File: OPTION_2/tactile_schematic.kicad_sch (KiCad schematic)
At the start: 58 parts, among them IC1 CY8C4145PVI-PS431, J1 Conn_01x02, J2 Conn_01x04, J3 Conn_01x04, J4 Conn_01x02, J5 Conn_ARM_SWD_TagConnect_TC203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

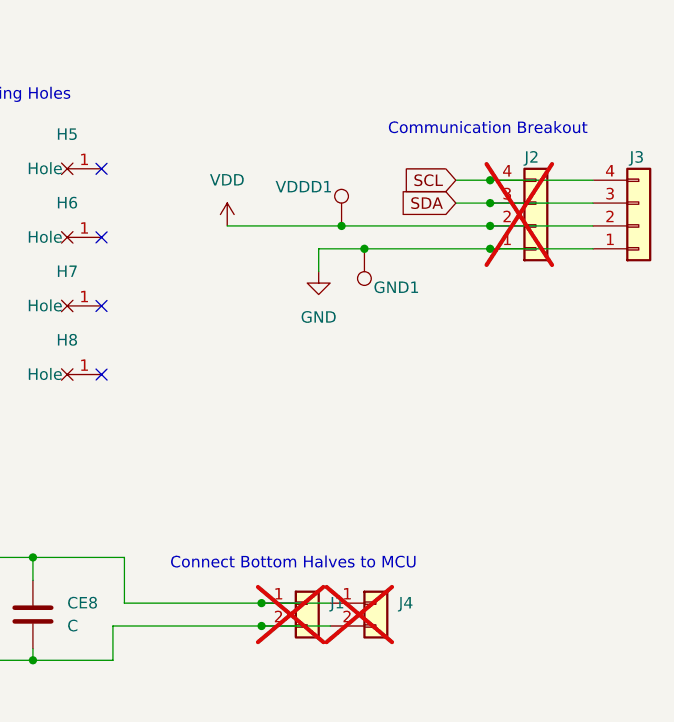
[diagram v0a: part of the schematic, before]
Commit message: three pcb trace configurations
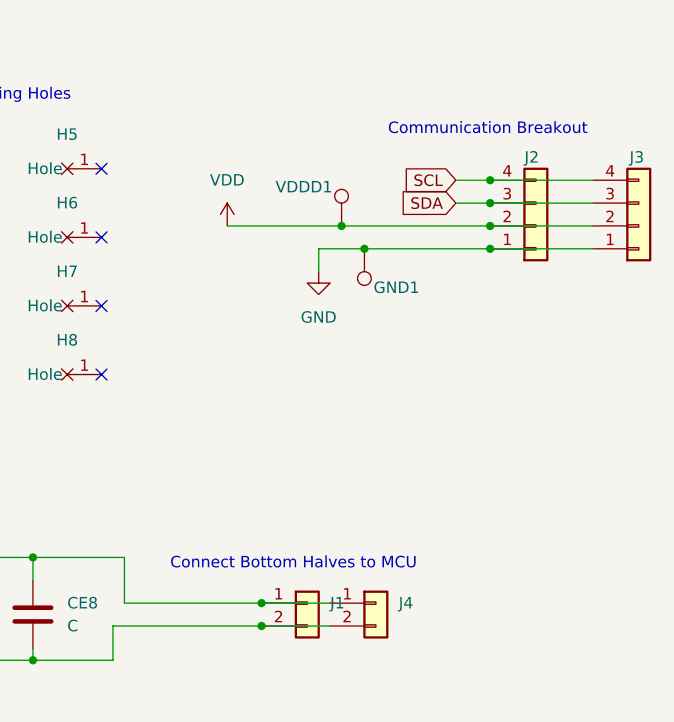
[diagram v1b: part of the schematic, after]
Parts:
- CE1, CE2, CE3, CE4: footprint ECE382N:COIL_GENERATOR -> ECE382N:04W_04S_COIL_BACK
- CE5, CE6, CE7, CE8: footprint ECE382N:COIL_GENERATOR -> ECE382N:04W_04S_COIL_FRONT
- J1, J2, J4: now fitted
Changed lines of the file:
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@@
 			)
 		)
-		(property "Footprint" "ECE382N:COIL_GENERATOR"
+		(property "Footprint" "ECE382N:04W_04S_COIL_BACK"
 			(at 39.0652 106.68 0)
 			(effects
@@
 			)
 		)
-		(property "Footprint" "ECE382N:COIL_GENERATOR"
+		(property "Footprint" "ECE382N:04W_04S_COIL_FRONT"
 			(at 192.7352 106.68 0)
 			(effects
@@
 		(in_bom yes)
 		(on_board yes)
-		(dnp yes)
+		(dnp no)
 		(fields_autoplaced yes)
 		(property "Reference" "J1"
@@
 			)
 		)
-		(property "Footprint" "ECE382N:COIL_GENERATOR"
+		(property "Footprint" "ECE382N:04W_04S_COIL_FRONT"
 			(at 181.3052 106.68 0)
 			(effects
@@
 			)
 		)
-		(property "Footprint" "ECE382N:COIL_GENERATOR"
+		(property "Footprint" "ECE382N:04W_04S_COIL_FRONT"
 			(at 204.1652 106.68 0)
 			(effects
@@
 		(in_bom yes)
 		(on_board yes)
-		(dnp yes)
+		(dnp no)
 		(property "Reference" "J2"
 			(at 257.81 52.07 0)
@@
 		(in_bom yes)
 		(on_board yes)
-		(dnp yes)
+		(dnp no)
 		(fields_autoplaced yes)
 		(property "Reference" "J4"
@@
 			)
 		)
-		(property "Footprint" "ECE382N:COIL_GENERATOR"
+		(property "Footprint" "ECE382N:04W_04S_COIL_BACK"
 			(at 121.6152 106.68 0)
 			(effects
@@
 			)
 		)
-		(property "Footprint" "ECE382N:COIL_GENERATOR"
+		(property "Footprint" "ECE382N:04W_04S_COIL_BACK"
 			(at 96.2152 106.68 0)
 			(effects
@@
 			)
 		)
-		(property "Footprint" "ECE382N:COIL_GENERATOR"
+		(property "Footprint" "ECE382N:04W_04S_COIL_FRONT"
 			(at 169.8752 106.68 0)
 			(effects
@@
 			)
 		)
-		(property "Footprint" "ECE382N:COIL_GENERATOR"
+		(property "Footprint" "ECE382N:04W_04S_COIL_BACK"
 			(at 67.0052 106.68 0)
 			(effects
